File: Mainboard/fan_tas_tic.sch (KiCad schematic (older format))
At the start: 80 parts, among them P1 CONN_01X04, P10 CONN_01X08, P11 CONN_01X04, P12 CONN_01X04, P13 CONN_01X04, P14 CONN_01X04, P2 CONN_01X04, P3 CONN_01X04, P4 CONN_01X04, P5 CONN_01X04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

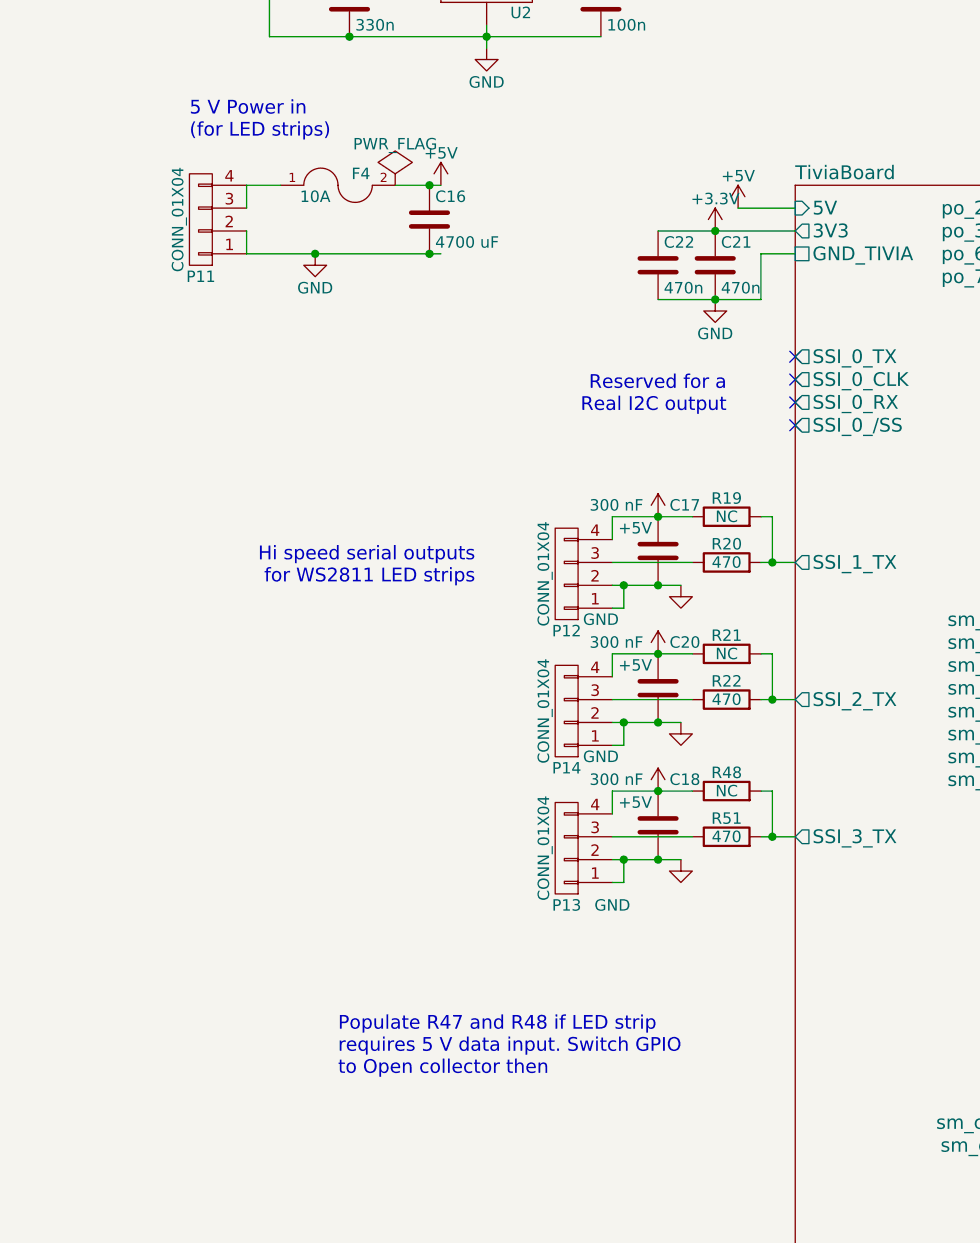
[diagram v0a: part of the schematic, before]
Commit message: Added 74HC04 buffer to WS2811 outputs
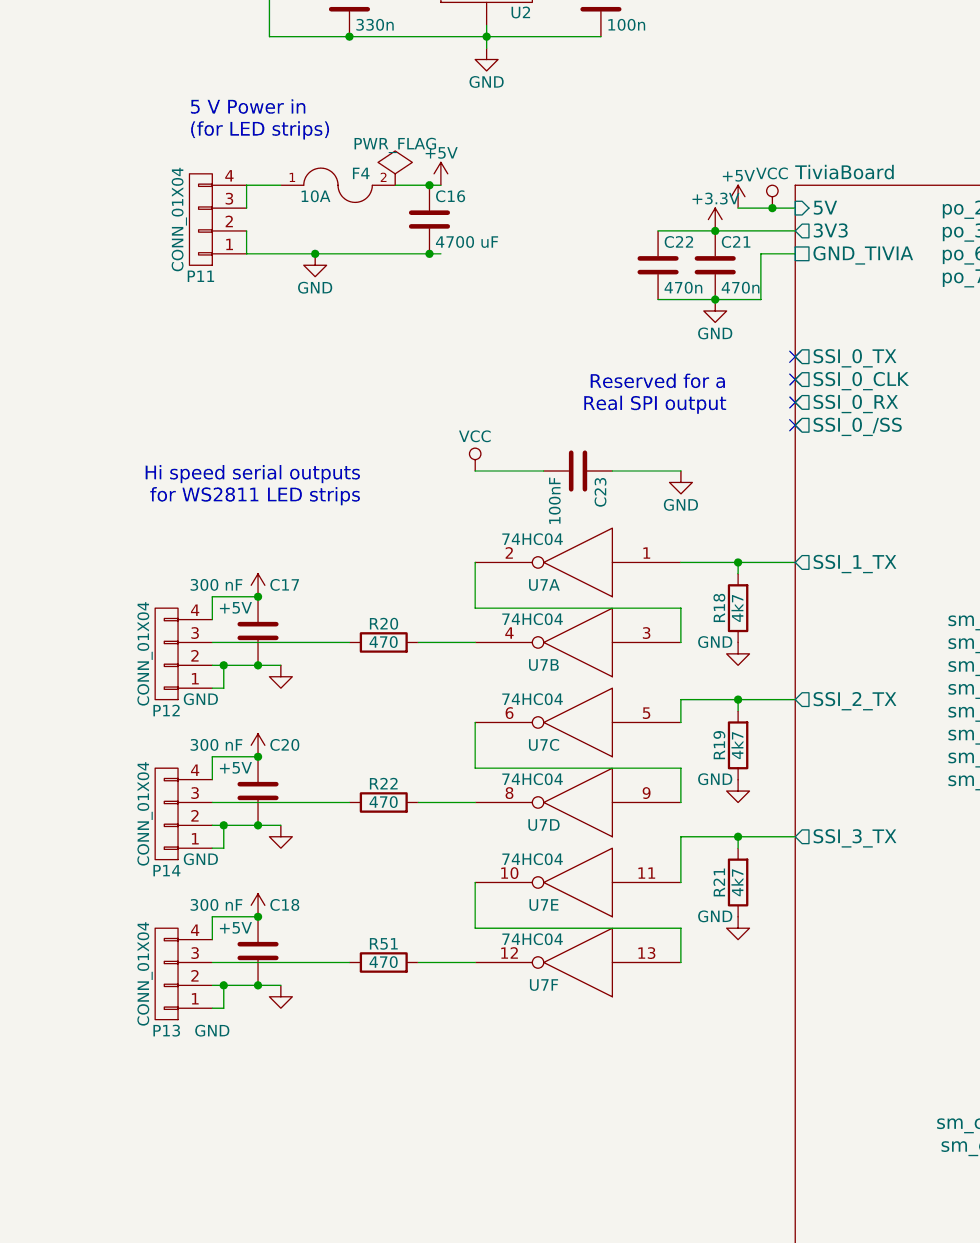
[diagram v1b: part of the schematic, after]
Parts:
- removed R48: NC, Resistors_ThroughHole:Resistor_Vertical_RM5mm, symbol R
- added C23: 100nF, Capacitors_SMD:C_0805_HandSoldering, symbol C
- added R18: 4k7, Resistors_ThroughHole:Resistor_Vertical_RM5mm, symbol R
- added U7: 74HC04, Housings_DIP:DIP-14_W7.62mm_LongPads, symbol 74HC04
- R19: value NC -> 4k7
- R21: value NC -> 4k7; footprint Resistors_ThroughHole:Resistor_Vertical_RM5mm -> Resistors_SMD:R_0805_HandSoldering
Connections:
- net +5V: now also C23.2, U7.14 (VCC), U7.14 (VCC), U7.14 (VCC), U7.14 (VCC), U7.14 (VCC), U7.14 (VCC); no longer R19.1, R21.1
- net GND: now also R19.1, R21.1, C23.1, R18.1, U7.7 (GND), U7.7 (GND), U7.7 (GND), U7.7 (GND), U7.7 (GND), U7.7 (GND)
- net TiviaBoard/SSI_1_TX: now also R18.2, U7.1; no longer R19.2, R20.2
- net TiviaBoard/SSI_2_TX: now also R19.2, U7.5; no longer R21.2, R22.2
- net TiviaBoard/SSI_3_TX: now also R21.2, U7.11; no longer R51.2
- new net: R51.2, U7.12
- new net: R22.2, U7.8
- new net: R20.2, U7.4
- new net: U7.2, U7.3
- new net: U7.6, U7.9
- new net: U7.10, U7.13
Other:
- note added: "Reserved for a\nReal SPI output"
- note removed: "Populate R47 and R48 if LED strip\nrequires 5 V data input. Switch GPIO\nto Open collector then"
- note removed: "Reserved for a\nReal I2C output"
- moved on the sheet: C17, C18, C20, P12, P13, P14, R20, R22, R51

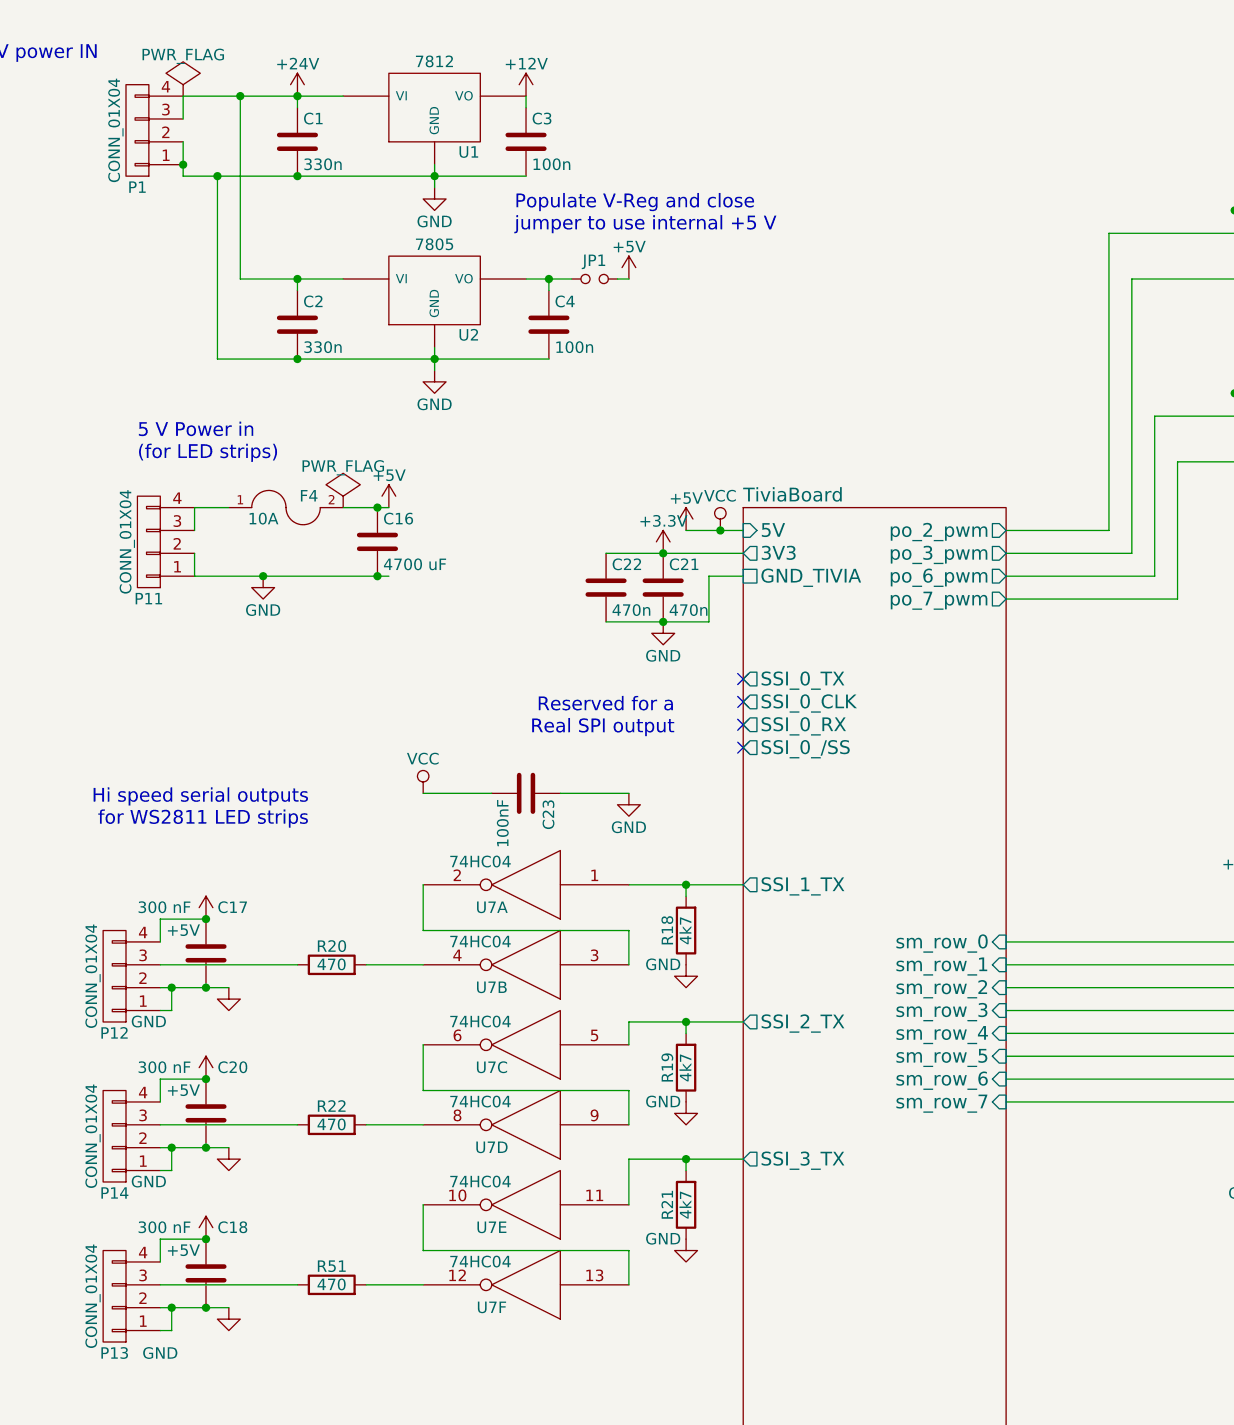
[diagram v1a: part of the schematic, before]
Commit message: Separated Tiva 5V from Power 5 V
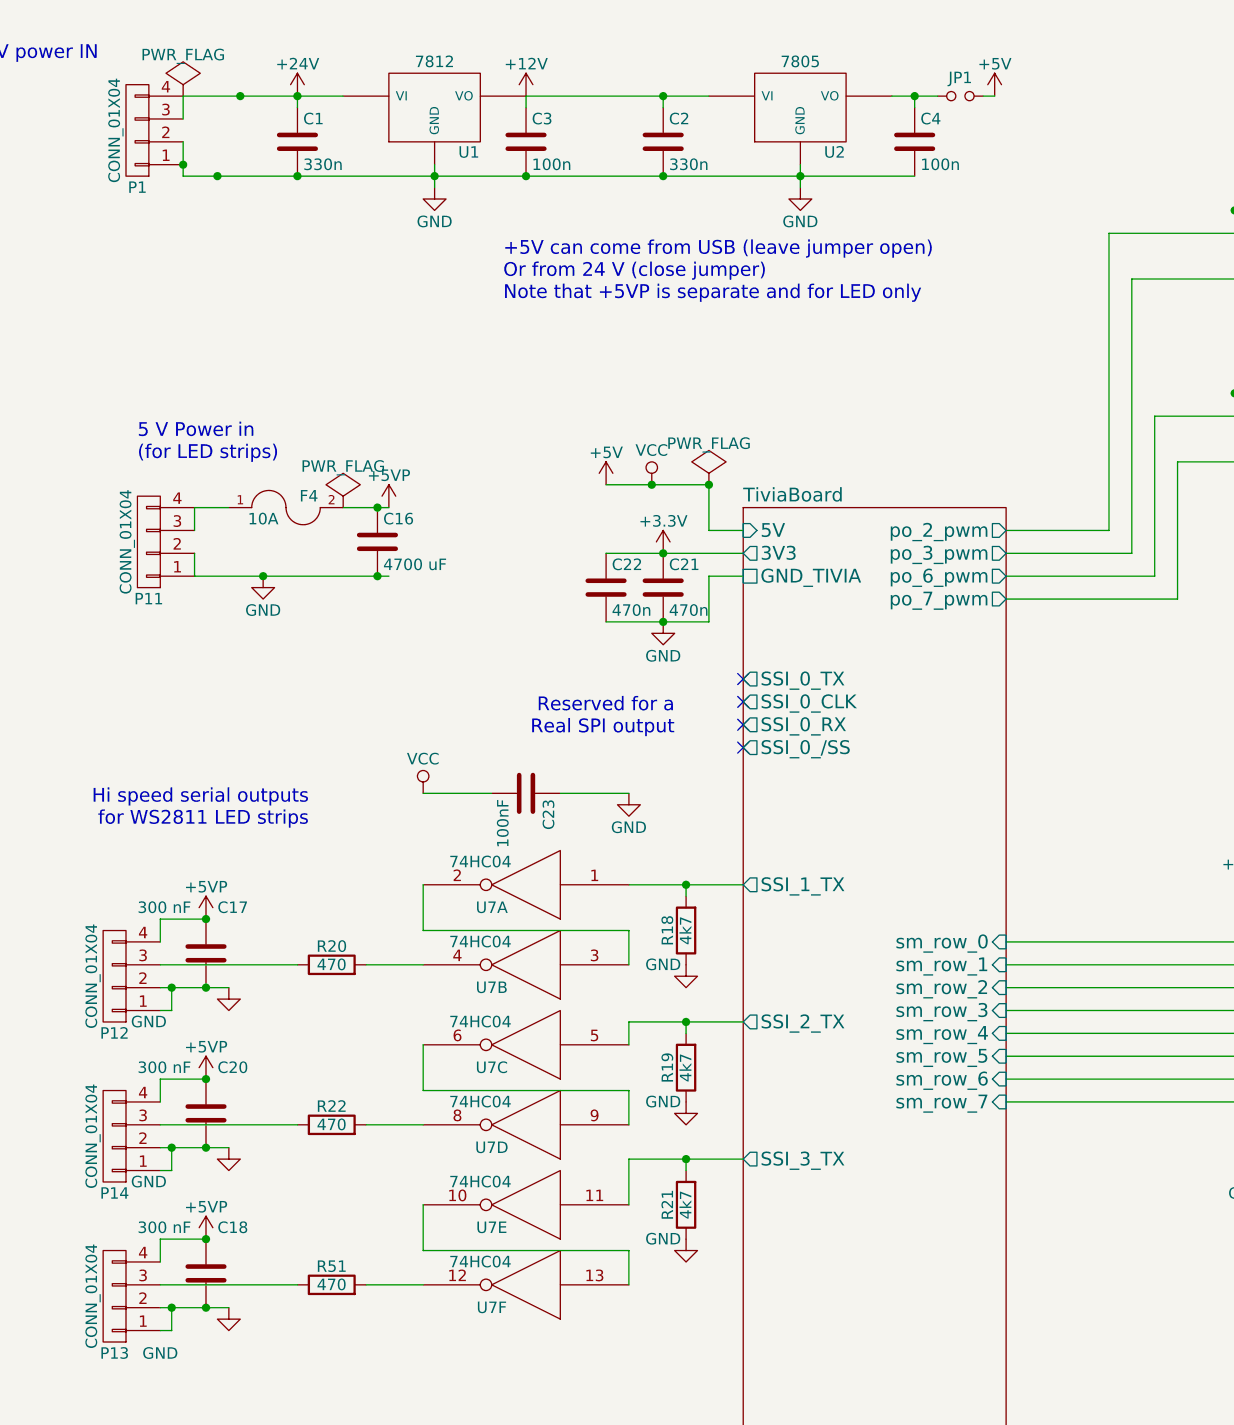
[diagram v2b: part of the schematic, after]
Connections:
- net +12V: now also C2.1, U2.VI
- net +24V: no longer C2.1, U2.VI
- net +5V: no longer C16.1, C17.1, C18.1, C20.1, F4.2, P12.4 (P4), P13.4 (P4), P14.4 (P4)
- new net +5VP: C16.1, C17.1, C18.1, C20.1, F4.2, P12.4 (P4), P13.4 (P4), P14.4 (P4)
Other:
- note added: "+5V can come from USB (leave jumper open)\nOr from 24 V (close jumper)\nNote that +5VP is separate and for LED only"
- note removed: "Populate V-Reg and close\njumper to use internal +5 V"
- moved on the sheet: C2, C4, JP1, U2

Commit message: Larger pads and vias to allow some alignment error
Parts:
- F1, F2, F3, F4: footprint Fuse_Holders_and_Fuses:Fuseholder5x20_horiz_open_lateral_Type-II -> Fuse_Holders_and_Fuses:Fuseholder5x20_horiz_open_universal_Type-III
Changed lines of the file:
@@
 F 0 "F1" H 9500 1350 50  0000 C CNN
 F 1 "FUSE" H 9300 1250 50  0000 C CNN
-F 2 "Fuse_Holders_and_Fuses:Fuseholder5x20_horiz_open_lateral_Type-II" H 9400 1300 50  0001 C CNN
+F 2 "Fuse_Holders_and_Fuses:Fuseholder5x20_horiz_open_universal_Type-III" H 9400 1300 50  0001 C CNN
 F 3 "" H 9400 1300 50  0000 C CNN
 	1    9400 1300
@@
 F 0 "F2" H 14550 1000 50  0000 C CNN
 F 1 "FUSE" H 14350 900 50  0000 C CNN
-F 2 "Fuse_Holders_and_Fuses:Fuseholder5x20_horiz_open_lateral_Type-II" H 14450 950 50  0001 C CNN
+F 2 "Fuse_Holders_and_Fuses:Fuseholder5x20_horiz_open_universal_Type-III" H 14450 950 50  0001 C CNN
 F 3 "" H 14450 950 50  0000 C CNN
 	1    14450 950
@@
 F 0 "F3" H 14550 3000 50  0000 C CNN
 F 1 "FUSE" H 14350 2900 50  0000 C CNN
-F 2 "Fuse_Holders_and_Fuses:Fuseholder5x20_horiz_open_lateral_Type-II" H 14450 2950 50  0001 C CNN
+F 2 "Fuse_Holders_and_Fuses:Fuseholder5x20_horiz_open_universal_Type-III" H 14450 2950 50  0001 C CNN
 F 3 "" H 14450 2950 50  0000 C CNN
 	1    14450 2950
@@
 F 0 "F4" H 2100 2950 50  0000 C CNN
 F 1 "10A" H 1900 2850 50  0000 C CNN
-F 2 "Fuse_Holders_and_Fuses:Fuseholder5x20_horiz_open_lateral_Type-II" H 2000 2900 50  0001 C CNN
+F 2 "Fuse_Holders_and_Fuses:Fuseholder5x20_horiz_open_universal_Type-III" H 2000 2900 50  0001 C CNN
 F 3 "" H 2000 2900 50  0000 C CNN
 	1    2000 2900

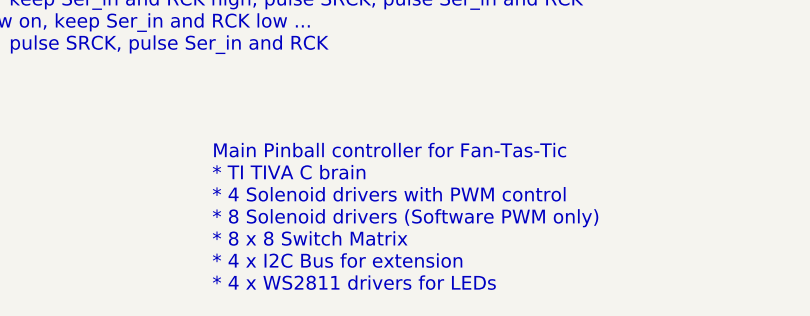
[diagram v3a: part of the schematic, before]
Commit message: Cleaned up traces
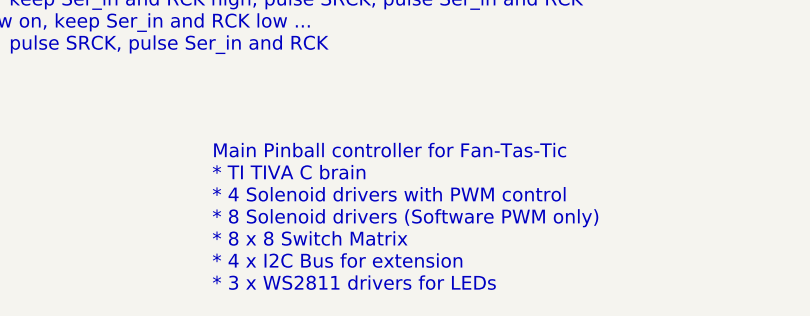
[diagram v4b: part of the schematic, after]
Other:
- note added: "Main Pinball controller for Fan-Tas-Tic\n* TI TIVA C brain\n* 4 Solenoid drivers with PWM control\n* 8 Solenoid drivers (Software PWM only)\n* 8 x 8 Switch Matrix\n* 4 x I2C Bus for extension\n* 3 x WS2811 drivers for LEDs\n"
- note removed: "Main Pinball controller for Fan-Tas-Tic\n* TI TIVA C brain\n* 4 Solenoid drivers with PWM control\n* 8 Solenoid drivers (Software PWM only)\n* 8 x 8 Switch Matrix\n* 4 x I2C Bus for extension\n* 4 x WS2811 drivers for LEDs\n"
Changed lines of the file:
@@
 $EndComp
 Text Notes 11900 10550 0    60   ~ 0
-Main Pinball controller for Fan-Tas-Tic\n* TI TIVA C brain\n* 4 Solenoid drivers with PWM control\n* 8 Solenoid drivers (Software PWM only)\n* 8 x 8 Switch Matrix\n* 4 x I2C Bus for extension\n* 4 x WS2811 drivers for LEDs\n
+Main Pinball controller for Fan-Tas-Tic\n* TI TIVA C brain\n* 4 Solenoid drivers with PWM control\n* 8 Solenoid drivers (Software PWM only)\n* 8 x 8 Switch Matrix\n* 4 x I2C Bus for extension\n* 3 x WS2811 drivers for LEDs\n
 $Comp
 L Jumper_NO_Small JP1

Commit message: Updated Schematic with minor changes after first prototype
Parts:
- added D10, D11, D12, D13, D14, D15, D16, D5, D6, D7, D8, D9: 1N5822, Diodes_ThroughHole:Diode_DO-201AD_Horizontal_RM15, symbol D_Schottky
- added D4: D_Schottky, Diodes_ThroughHole:Diode_DO-201AD_Horizontal_RM15, symbol D_Schottky
- added JP2: Jumper_NO_Small, Pin_Headers:Pin_Header_Straight_1x02, symbol Jumper_NO_Small
- added K1: RELAY_2RT, Relays_ThroughHole:Relay_DPDT_Schrack-RT2_RM5mm, symbol RELAY_2RT
- added Q21: BSS138, TO_SOT_Packages_SMD:SOT-23, symbol BSS138
- added R47: 4k7, Resistors_ThroughHole:Resistor_Vertical_RM5mm, symbol R
- R1, R14, R2, R5: value 47R -> 200R
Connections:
- net +12V: now also K1.8
- net +24V: now also K1.16 (T2); no longer C1.1, P1.3 (P3), P1.4 (P4), U1.VI
- net +5V: now also JP2.2
- net +5VP: now also JP2.1
- net GND: now also D4.2 (A), Q21.2 (S)
- net powerChannel10/Drain: now also D15.2 (A)
- net powerChannel11/Drain: now also D16.2 (A)
- net powerChannel4/Drain: now also D9.2 (A)
- net powerChannel5/Drain: now also D10.2 (A)
- net powerChannel6/Drain: now also D11.2 (A)
- net powerChannel7/Drain: now also D12.2 (A)
- net powerChannel8/Drain: now also D13.2 (A)
- net powerChannel9/Drain: now also D14.2 (A)
- net at C12.1, F1.2, P7.1 (P1)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: now also D5.1 (K), D6.1 (K), D7.1 (K), D8.1 (K)
- net at P7.2 (P2), Q1.2 (D): now also D5.2 (A)
- net at P7.4 (P4), Q2.2 (D): now also D6.2 (A)
- net at P7.6 (P6), Q3.2 (D): now also D7.2 (A)
- net at P7.8 (P8), Q4.2 (D): now also D8.2 (A)
- net at C14.1, F2.2, P9.1 (P1)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: now also D10.1 (K), D11.1 (K), D12.1 (K), D9.1 (K)
- net at C15.1, F3.2, P10.1 (P1)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: now also D13.1 (K), D14.1 (K), D15.1 (K), D16.1 (K)
- new net: C1.1, K1.12 (C2), P1.3 (P3), P1.4 (P4), U1.VI
- new net: D4.1 (K), K1.9, Q21.3 (D)
- new net: Q21.1 (G), R47.2
- new net TiviaBoard/PE0_24V_ENABLE: R47.1
- no-connect marks 6 -> 10
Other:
- note added: "+5V can come from:\n * USB (leave both jumpers open)\n * LED supply (close JP2)\n * 24 V solenoid supply (close JP1)"
- note added: "Set jumper to power\nTiva from LED supply"
- note added: "This relays disables the 24 V supply line for the\nsolenoids, until explicitly enabled by the higher\nlevel software."
- note added: "ToDo:\n* Move USB DEBUG aout of the way!\n* Add more decoupling!"
- note removed: "+5V can come from USB (leave jumper open)\nOr from 24 V (close jumper)\nNote that +5VP is separate and for LED only"
- moved on the sheet: C12, C15, C16, C17, C18, C20, C23, F1, F2, F3, F4, P1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
